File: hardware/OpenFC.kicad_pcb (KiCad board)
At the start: 6 copper layers, 26.9 x 26.9 mm, 131 parts, among them J10 5V, J12 5V, J14 5V, J15 5V, J17 5V, J18 5V, J20 5V, J21 5V, J22 5V, J24 5V, J25 5V, J26 5V, J27 5V, J28 5V, J29 5V, J30 5V, J31 5V, J32 5V, J33 5V, J34 5V, J35 5V, J37 5V, J39 5V, J40 5V, J41 5V, J42 5V, J43 5V, J44 5V, J45 5V, J46 5V, J48 5V, J49 5V, J5 5V, J8 5V, P1 SM08B-SRSS-TB(LF)(SN), Q5 AP1606, Q6 AP1606, U1 COS8051SOT, U10 RP2354A, U11 TS2306A 240GF MSM 9_C2976675, U12 LP5912-1.8DRVR, U18 SN74LVC1G3157DTBR, U2 TLV7031DPWR, U3 LMR51430YFDDCR, U4 LMR51430YFDDCR, U7 LP5912-3.3DRVR, U8 SM06B-SRSS-TB(LF)(SN), U9 BMI270, X1 XTM25012000JT00351001

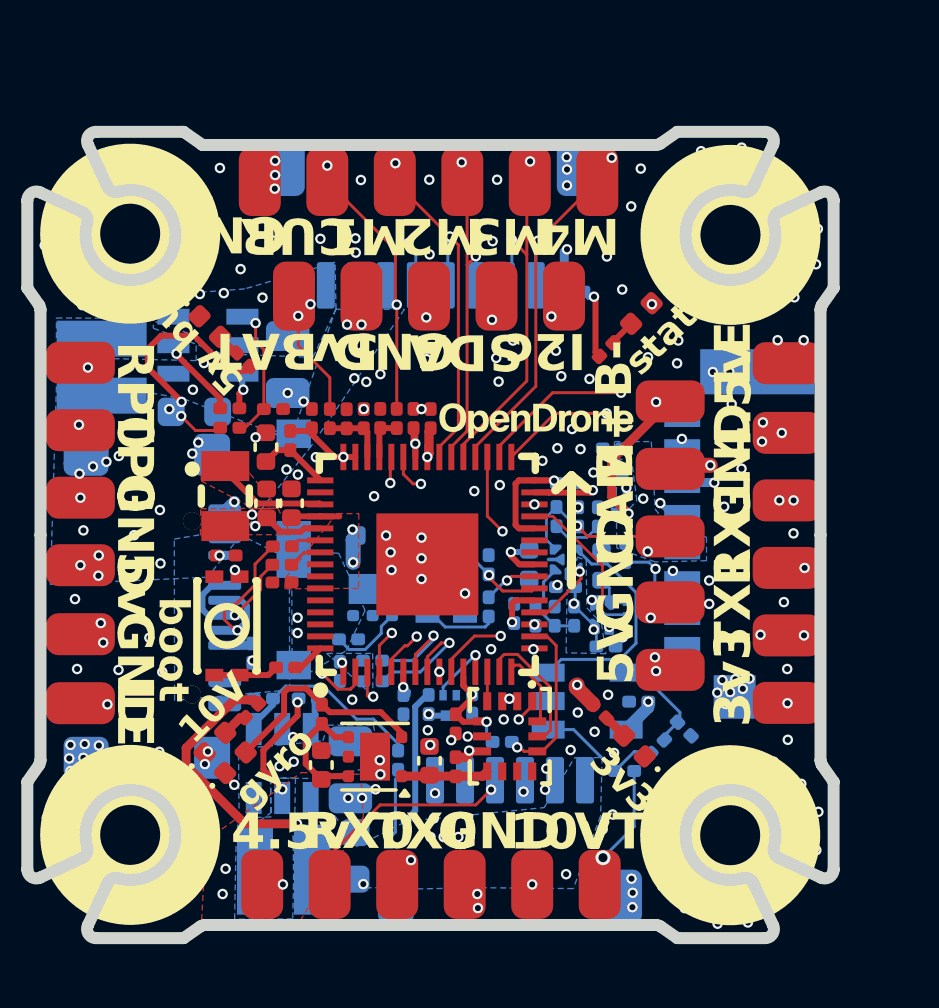
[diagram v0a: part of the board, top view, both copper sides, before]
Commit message: switch to 0.1mm trace width and spacing for more options in PCB printing
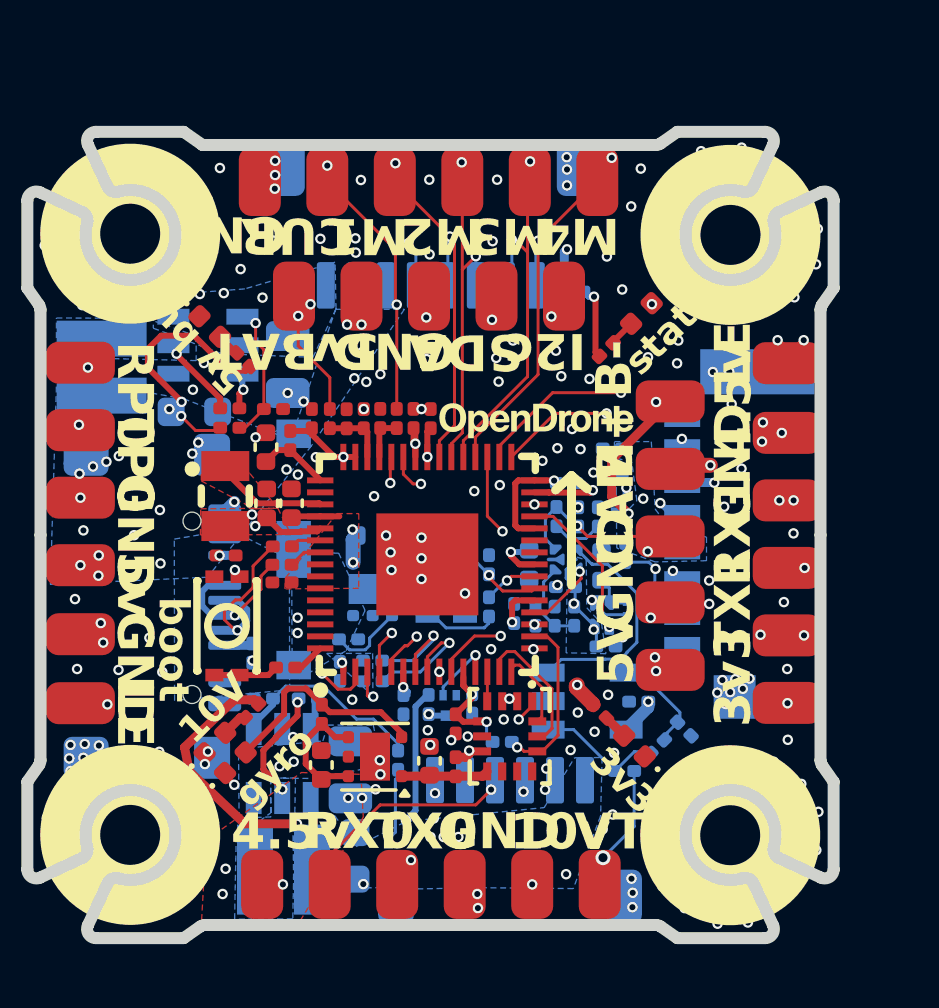
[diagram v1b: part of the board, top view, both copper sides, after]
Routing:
- net +3.3V: track 31.5 -> 30.6 mm
- net /PADS/M2: track 10.8 -> 11.5 mm
